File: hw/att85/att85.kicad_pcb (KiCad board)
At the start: 2 copper layers, 80 x 40 mm, 45 parts, among them J101 Barrel_Jack_Switch, J102 Screw_Terminal_01x03, J103 AVR-ISP-6, J104 Conn_01x02, J105 Conn_01x02, Q101 BC817, SW101 SW_Push, SW102 SW_Push, SW103 SW_Push, SW104 SW_Push, SW105 SW_Push, SW106 SW_Push, U101 ATtiny85-20P, U102 MT3608-MODULE, U105 74AHC1G125

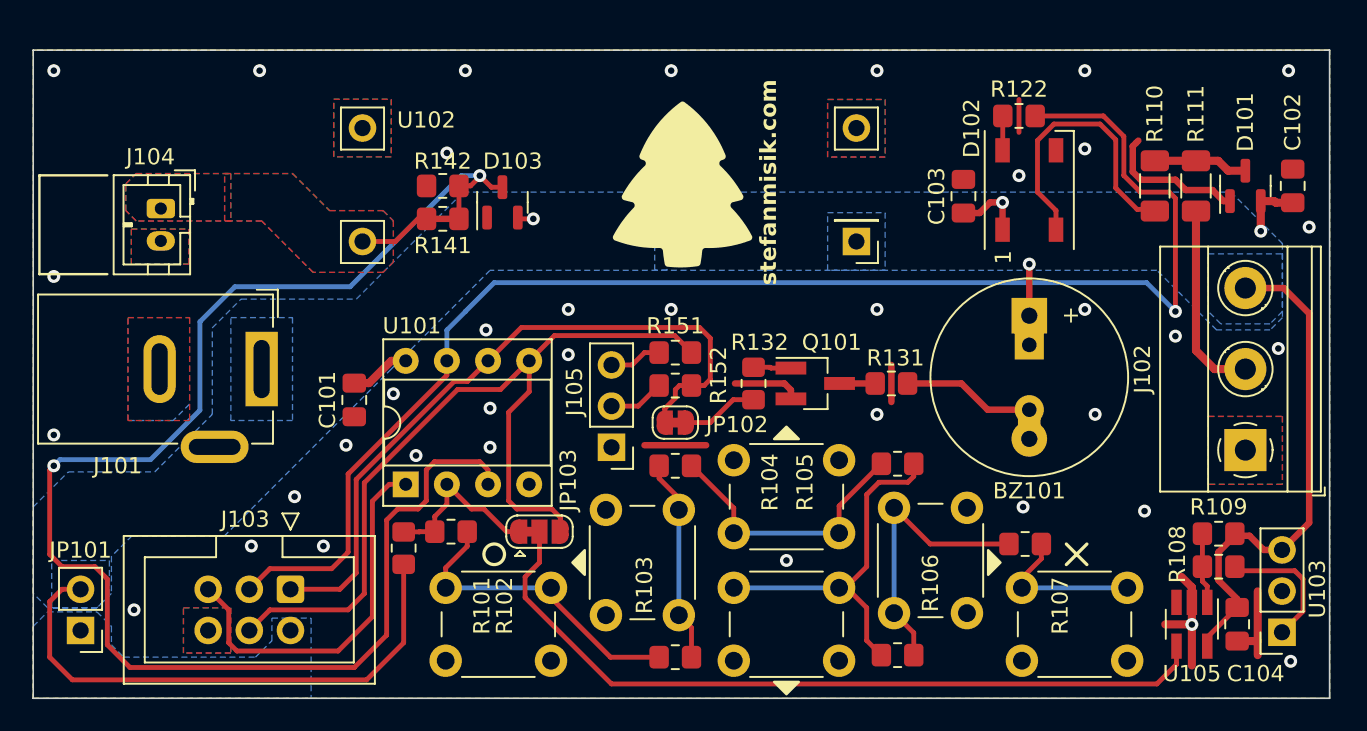
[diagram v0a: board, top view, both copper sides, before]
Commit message: feat(hw): remove unused components, wire IR to separate uC pin
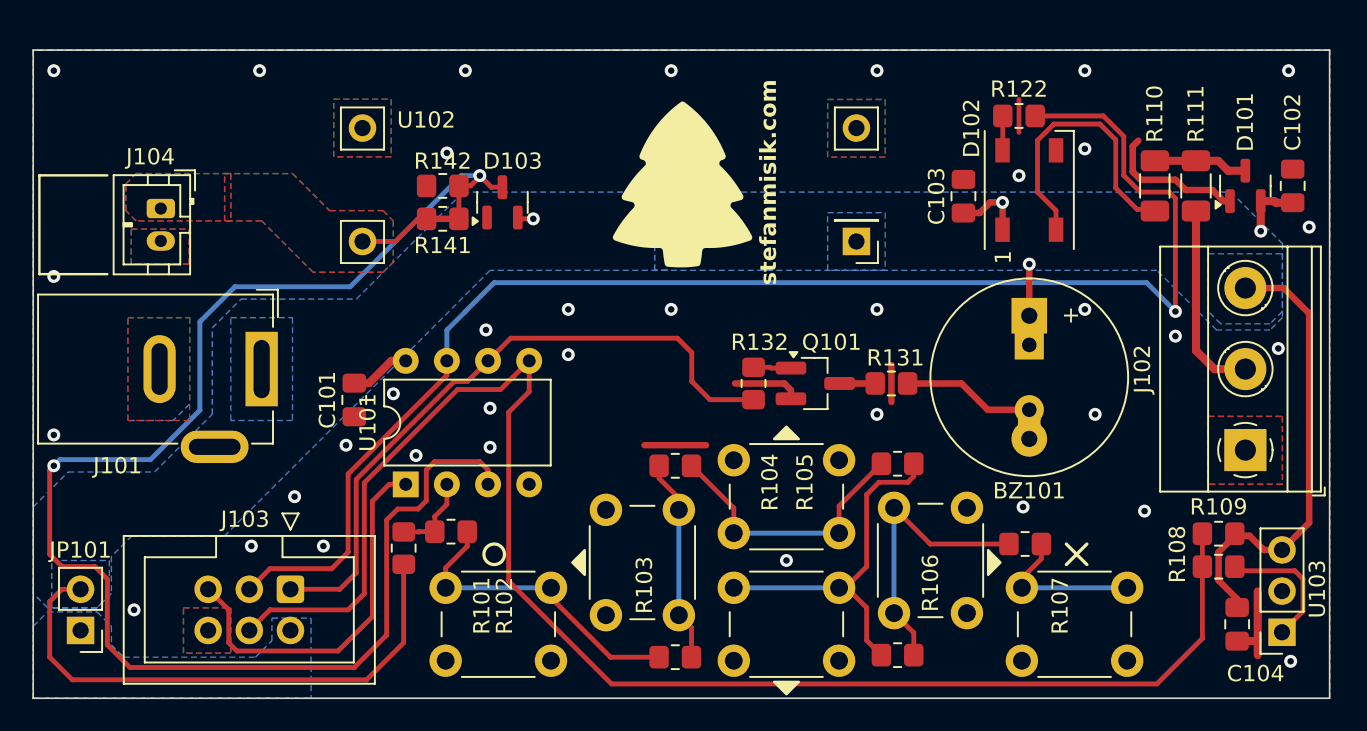
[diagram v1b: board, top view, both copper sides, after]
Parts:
- removed J105: Conn_01x02, Connector_PinHeader_2.54mm:PinHeader_1x03_P2.54mm_Vertical
- removed JP102: Jumper_2_Bridged, Jumper:SolderJumper-2_P1.3mm_Bridged_RoundedPad1.0x1.5mm
- removed JP103: Jumper_3_Bridged12, Jumper:SolderJumper-3_P1.3mm_Bridged12_RoundedPad1.0x1.5mm
- removed R151, R152: 330R, Resistor_SMD:R_0805_2012Metric_Pad1.20x1.40mm_HandSolder
- removed U105: 74AHC1G125, Package_TO_SOT_SMD:SOT-23-5_HandSoldering
- U101: footprint Package_DIP:DIP-8_W7.62mm_Socket -> Package_DIP:DIP-8_W7.62mm
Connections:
- net /KEYPAD_ADC/IR renamed /KEYPAD_ADC
- J103 pad 1: /BUZZER/TX/MISO -> /BUZZER/MISO
- J103 pad 4: /RX/MOSI -> /IR/MOSI
- R108 pad 1: Net-(R108-Pad1) -> /IR/MOSI
- R109 pad 1: Net-(R108-Pad1) -> /IR/MOSI
- R132 pad 1: /BUZZER -> /BUZZER/MISO
- U101 pad 5: /RX/MOSI -> /IR/MOSI
- U101 pad 6: /BUZZER/TX/MISO -> /BUZZER/MISO
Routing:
- net /IR/MOSI: track 0.00 -> 95.2 mm
- net /RX/MOSI: track 52.9 -> 0.00 mm
- net Net-(JP103-C): track 48.5 -> 0.00 mm
- net /BUZZER/TX/MISO: track 43.5 -> 0.00 mm
- net /BUZZER/MISO: track 0.00 -> 41.0 mm
- net GND: track 33.7 -> 26.4 mm, vias 37 -> 36
- net /KEYPAD_ADC: track 10.8 -> 5.16 mm
- net /BUZZER: track 4.76 -> 0.00 mm
- net Net-(R108-Pad1): track 4.23 -> 0.00 mm
- net Net-(J105-Pin_2): track 3.46 -> 0.00 mm
- net Net-(J105-Pin_3): track 3.25 -> 0.00 mm
- net +5V: track 81.6 -> 78.5 mm

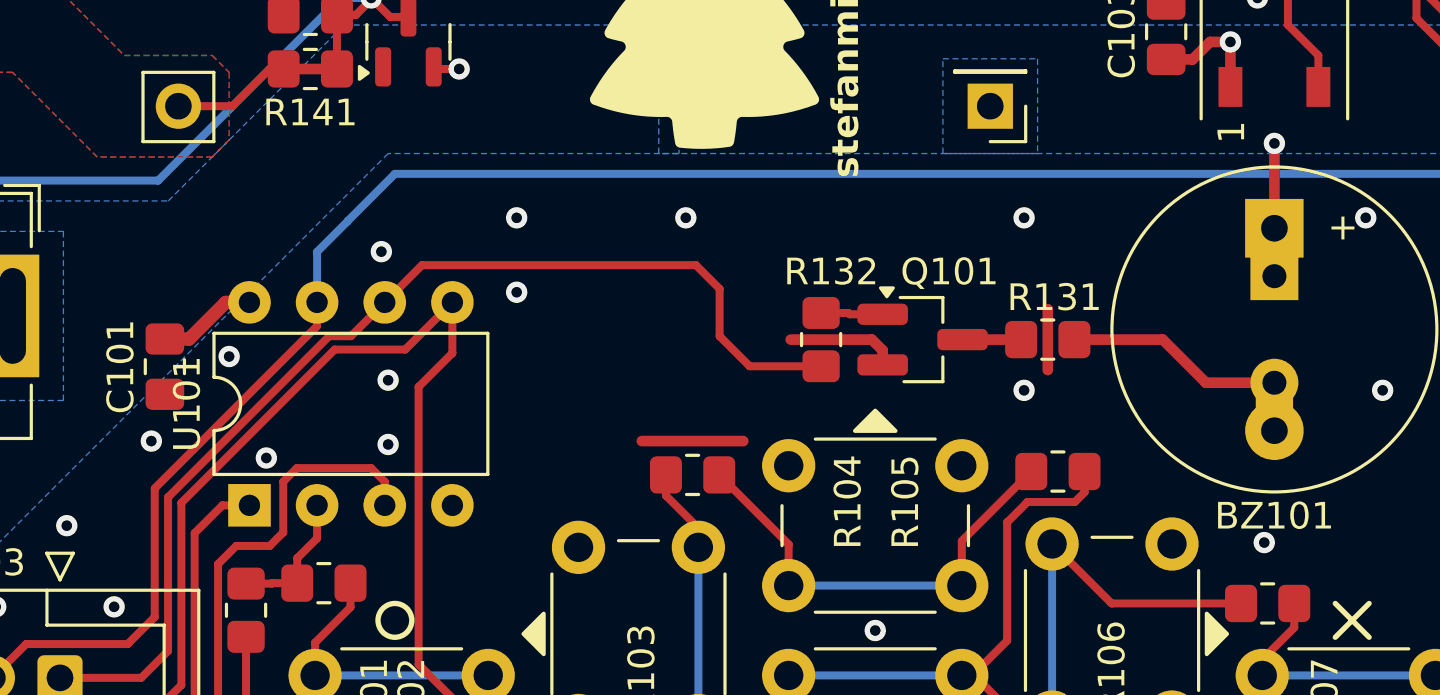
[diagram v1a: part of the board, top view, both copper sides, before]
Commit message: feat(hw): improve layout and add a mounting hole
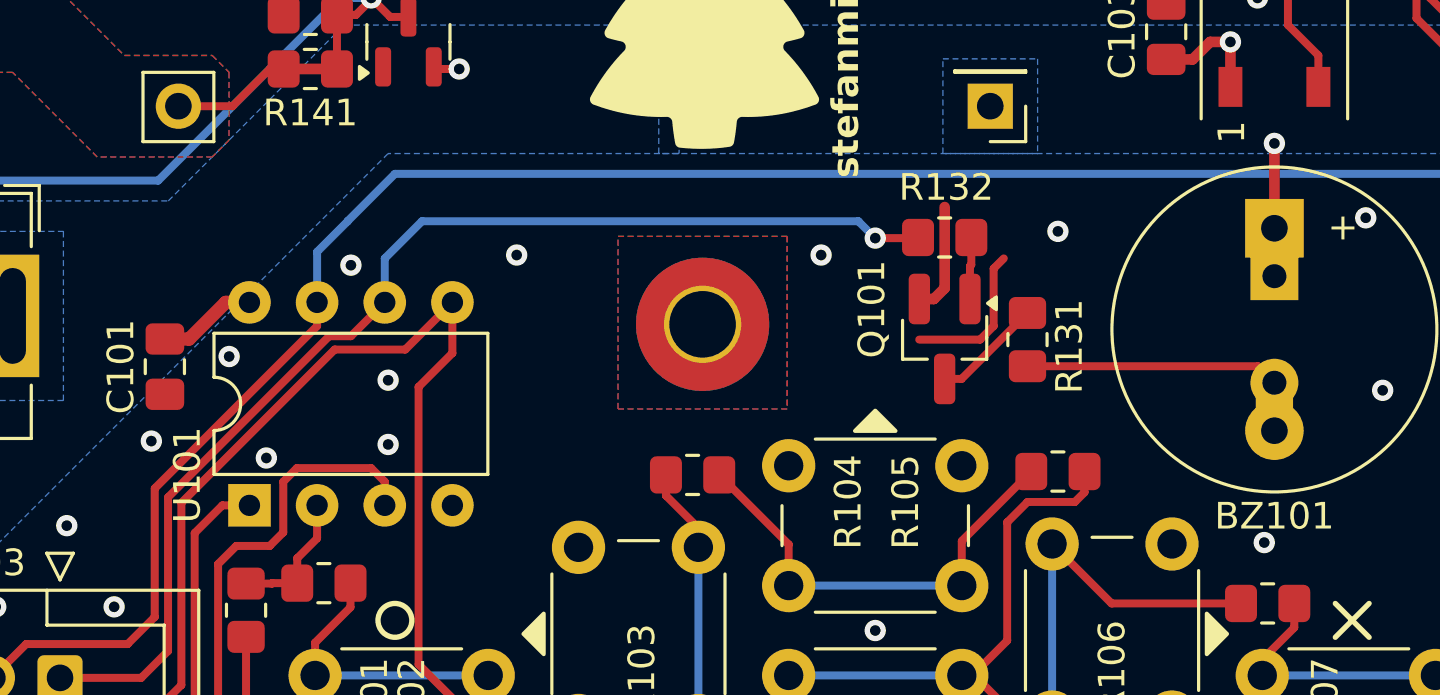
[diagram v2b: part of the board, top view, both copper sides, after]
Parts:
- added H1: MountingHole_Pad, MountingHole:MountingHole_2.5mm_Pad_TopBottom, F.Cu at (159.4, 94.9)
- moved R132 6.02 mm to (168.5, 91.7), turned to 0 degrees
- moved Q101 0.83 mm to (168.5, 95.5), turned to -90 degrees
- moved R131 0.76 mm to (171.6, 95.5), turned to 90 degrees
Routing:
- net /BUZZER/MISO: track 41.0 -> 43.9 mm, vias 0 -> 1
- net Net-(Q101-C): track 2.20 -> 4.13 mm
- net Net-(BZ101--): track 8.18 -> 9.53 mm
- net GND: track 26.4 -> 26.0 mm, vias 36 -> 34

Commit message: fix(hw): minor improvements
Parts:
- added C105: 10u, Capacitor_SMD:C_1206_3216Metric_Pad1.33x1.80mm_HandSolder, F.Cu at (190.5, 106.6)
- R109: value 10K -> 20K
- U103: value ~ -> VS1838B
- moved R109 7.90 mm to (191.9, 112.6)
- moved R108 3.86 mm to (191.9, 110.6)
- moved C104 3.30 mm to (192.8, 107.2)
- moved U103 0.38 mm to (196.1, 110.9)
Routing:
- net +5V: track 78.5 -> 91.1 mm
- net Net-(U103-OUT): track 8.35 -> 3.26 mm
- net /IR/MOSI: track 95.2 -> 90.2 mm
- net GND: track 26.0 -> 27.6 mm

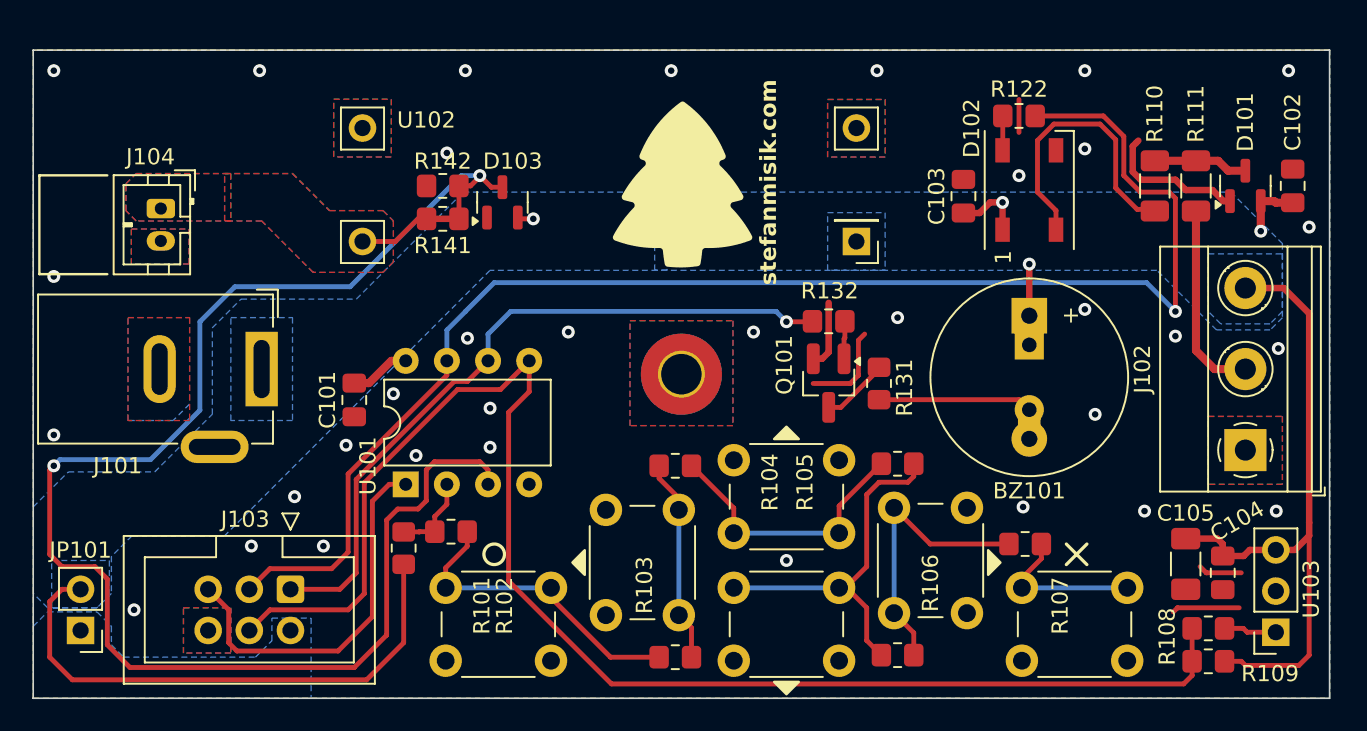
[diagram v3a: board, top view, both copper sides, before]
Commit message: refactor(hw): add rounded corners
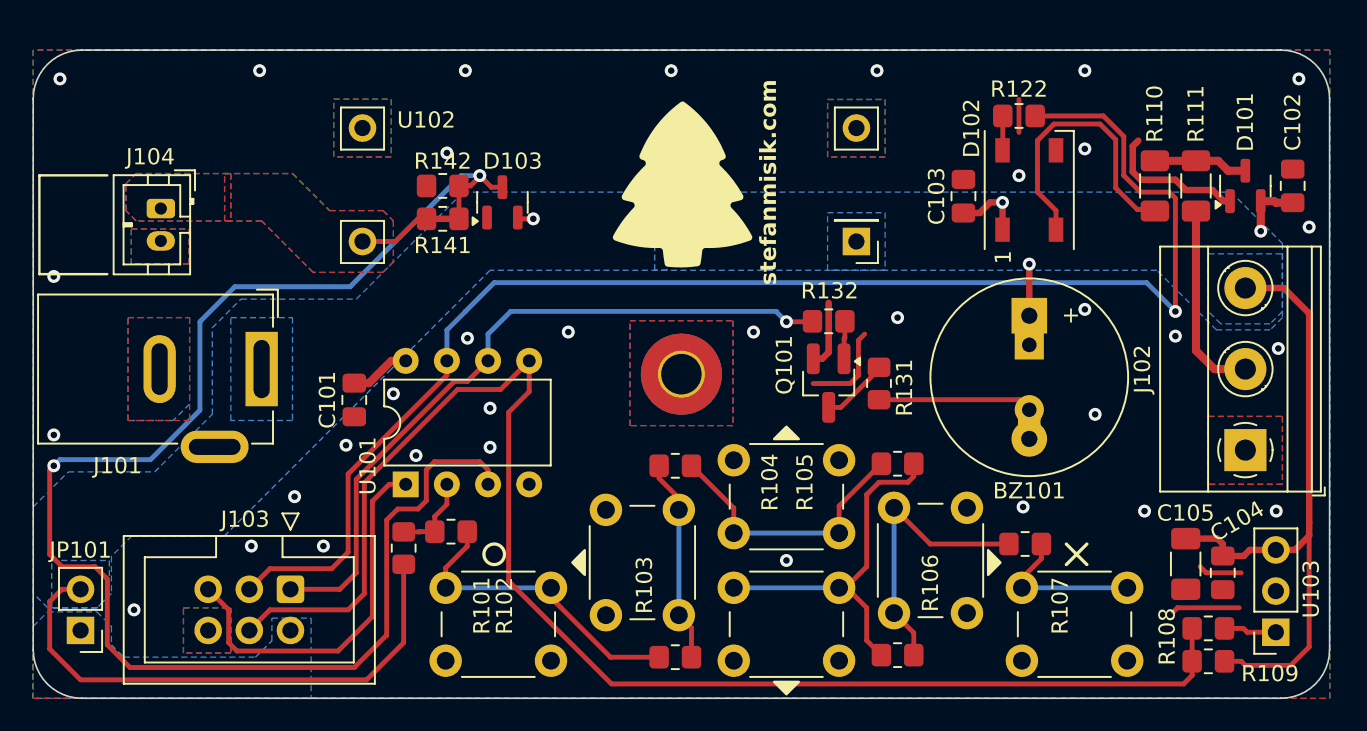
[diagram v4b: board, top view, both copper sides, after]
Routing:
- net +5V: track 91.1 -> 90.5 mm
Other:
- outline, holes or cut-outs redrawn
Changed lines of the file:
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@@
 		(layer "F.SilkS")
 	)
-	(gr_rect
-		(start 119.38 74.93)
-		(end 199.38 114.93)
+	(gr_line
+		(start 196.38 74.93)
+		(end 122.38 74.93)
 		(stroke
 			(width 0.1)
 			(type default)
 		)
-		(fill none)
 		(layer "Edge.Cuts")
 	)
+	(gr_line
+		(start 122.38 114.93)
+		(end 196.38 114.93)
+		(stroke
+			(width 0.1)
+			(type default)
+		)
+		(layer "Edge.Cuts")
+	)
+	(gr_line
+		(start 199.38 111.93)
+		(end 199.38 77.93)
+		(stroke
+			(width 0.1)
+			(type default)
+		)
+		(layer "Edge.Cuts")
+	)
+	(gr_line
+		(start 119.38 77.93)
+		(end 119.38 111.93)
+		(stroke
+			(width 0.1)
+			(type default)
+		)
+		(layer "Edge.Cuts")
+	)
+	(gr_arc
+		(start 119.38 77.93)
+		(mid 120.25868 75.80868)
+		(end 122.38 74.93)
+		(stroke
+			(width 0.1)
+			(type default)
+		)
+		(layer "Edge.Cuts")
+	)
+	(gr_arc
+		(start 122.38 114.93)
+		(mid 120.25868 114.05132)
+		(end 119.38 111.93)
+		(stroke
+			(width 0.1)
+			(type default)
+		)
+		(layer "Edge.Cuts")
+	)
+	(gr_arc
+		(start 196.38 74.93)
+		(mid 198.50132 75.80868)
+		(end 199.38 77.93)
+		(stroke
+			(width 0.1)
+			(type default)
+		)
+		(layer "Edge.Cuts")
+	)
+	(gr_arc
+		(start 199.38 111.93)
+		(mid 198.50132 114.05132)
+		(end 196.38 114.93)
+		(stroke
+			(width 0.1)
+			(type default)
+		)
+		(layer "Edge.Cuts")
+	)
 	(gr_text "JLCJLCJLCJLC"
-		(at 188.407 114.427 0)
+		(at 186.563 76.835 0)
 		(layer "B.SilkS")
 		(effects
@@
 	)
 	(segment
-		(start 194.183 112.903)
-		(end 197.485 112.903)
+		(start 122.301 108.204)
+		(end 121.158 108.204)
 		(width 0.3)
 		(layer "F.Cu")
@@
 	)
 	(segment
-		(start 120.396 112.395)
-		(end 121.793 113.792)
-		(width 0.3)
+		(start 194.183 112.903)
+		(end 196.977 112.903)
+		(width 0.3)
+		(layer "F.Cu")
+		(net 1)
+	)
+	(segment
+		(start 192.897 112.649)
+		(end 193.929 112.649)
+		(width 0.3)
+		(layer "F.Cu")
+		(net 1)
+	)
+	(segment
+		(start 192.786 106.1505)
+		(end 194.0775 106.1505)
+		(width 0.4)
+		(layer "F.Cu")
+		(net 1)
+	)
+	(segment
+		(start 179.198 86.016)
+		(end 179.198 84.329)
+		(width 0.4)
+		(layer "F.Cu")
+		(net 1)
+	)
+	(segment
+		(start 180.848 88.138)
+		(end 180.848 91.323)
+		(width 0.4)
 		(layer "F.Cu")
 		(net 1)
@@
 	)
 	(segment
-		(start 192.786 106.1505)
-		(end 194.0775 106.1505)
-		(width 0.4)
-		(layer "F.Cu")
-		(net 1)
-	)
-	(segment
-		(start 179.198 86.016)
-		(end 179.198 84.329)
-		(width 0.4)
-		(layer "F.Cu")
-		(net 1)
-	)
-	(segment
-		(start 180.848 88.138)
-		(end 180.848 91.323)
-		(width 0.4)
-		(layer "F.Cu")
-		(net 1)
-	)
-	(segment
-		(start 120.396 108.966)
-		(end 120.396 112.395)
+		(start 139.954 113.792)
+		(end 142.24 111.506)
+		(width 0.3)
+		(layer "F.Cu")
+		(net 1)
+	)
+	(segment
+		(start 193.929 112.649)
+		(end 194.183 112.903)
+		(width 0.3)
+		(layer "F.Cu")
+		(net 1)
+	)
+	(segment
+		(start 196.549 89.615)
+		(end 194.183 89.615)
+		(width 0.4)
+		(layer "F.Cu")
+		(net 1)
+	)
+	(segment
+		(start 196.977 112.903)
+		(end 198.12 111.76)
 		(width 0.3)
 		(layer "F.Cu")
@@
 	)
 	(segment
-		(start 196.549 89.615)
-		(end 194.183 89.615)
-		(width 0.4)
-		(layer "F.Cu")
-		(net 1)
-	)
-	(segment
-		(start 122.301 108.204)
-		(end 121.158 108.204)
-		(width 0.3)
-		(layer "F.Cu")
-		(net 1)
-	)
-	(segment
 		(start 192.786 106.1505)
 		(end 192.786 105.41)
@@
 	)
 	(segment
-		(start 197.485 112.903)
-		(end 198.12 112.268)
-		(width 0.3)
-		(layer "F.Cu")
-		(net 1)
-	)
-	(segment
-		(start 193.929 112.649)
-		(end 194.183 112.903)
-		(width 0.3)
-		(layer "F.Cu")
-		(net 1)
-	)
-	(segment
 		(start 149.3645 85.344)
 		(end 149.286 85.2655)
@@
 		(end 192.455 105.079)
 		(width 0.4)
-		(layer "F.Cu")
-		(net 1)
-	)
-	(segment
-		(start 121.793 113.792)
-		(end 139.954 113.792)
-		(width 0.3)
 		(layer "F.Cu")
 		(net 1)
@@
 	)
 	(segment
+		(start 122.301 113.792)
+		(end 139.954 113.792)
+		(width 0.3)
+		(layer "F.Cu")
+		(net 1)
+	)
+	(segment
 		(start 195.133 86.106)
 		(end 195.133 84.2495)
@@
 	)
 	(segment
-		(start 192.897 112.649)
-		(end 193.929 112.649)
-		(width 0.3)
-		(layer "F.Cu")
-		(net 1)
-	)
-	(segment
-		(start 139.954 113.792)
-		(end 142.24 111.506)
+		(start 120.396 108.966)
+		(end 120.396 111.887)
+		(width 0.3)
+		(layer "F.Cu")
+		(net 1)
+	)
+	(segment
+		(start 120.396 111.887)
+		(end 122.301 113.792)
+		(width 0.3)
+		(layer "F.Cu")
+		(net 1)
+	)
+	(segment
+		(start 198.12 111.76)
+		(end 198.12 104.1)
 		(width 0.3)
 		(layer "F.Cu")
@@
 	)
 	(segment
-		(start 198.12 112.268)
-		(end 198.12 104.1)
-		(width 0.3)
-		(layer "F.Cu")
-		(net 1)
-	)
-	(segment
 		(start 195.133 84.2495)
 		(end 195.961 84.2495)
@@
 	)
 	(via
-		(at 120.65 76.2)
+		(at 121.031 76.708)
 		(size 0.8)
 		(drill 0.4)
@@
 	)
 	(via
-		(at 196.85 76.2)
-		(size 0.8)
-		(drill 0.4)
+		(at 197.485 76.708)
+		(size 0.8)
+		(drill 0.4)
